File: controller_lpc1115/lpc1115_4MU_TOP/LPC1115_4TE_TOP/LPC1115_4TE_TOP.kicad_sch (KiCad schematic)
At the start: 101 parts, among them P1 ML26, P2 ISP, P3 FE12-1, Q1 BC856, Q2 FZT753, Q3 BC847, U1 LPC1115FBD48, U2 BD9G101, U3 12MHz

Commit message: update all stuff
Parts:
- added D10: 1N4148W, Diode_SMD:D_SOD-123, symbol Diode:1N4148W
- added R3: 390k, Resistor_SMD:R_0805_2012Metric, symbol Device:R
- added R4: 43k, Resistor_SMD:R_0805_2012Metric, symbol Device:R
- C1: value 15nF -> 15n
- C10, C11, C14, C21, C5, C8: value 100nF -> 100n
- C13, C24: value 1uF -> 1u
- C15, C18: value 100pF -> 100p
- C16, C17, C19: value 10nF -> 10n
- C2: value 470n -> 270n; now not fitted
- C22: value 220pF -> 220p
- C3: value VF 100/35 K-D8 -> 100µ/35V
- C4: value 4.7uF 50V -> 4.7µ/35V
- C6: value 47uF 10V -> 47µ/10V
- C7: value 100uF -> 100µ/10V
- D1, D11, D12, D14, D17, D2, D3, D4, D5, D6, D7, D8: value CD4148W -> 1N4148W; footprint Diode_SMD:D_0805_2012Metric -> Diode_SMD:D_SOD-123; symbol Diode:CD4148W -> Diode:1N4148W
- D13: value SMAJ40AC -> SMAJ40CA; now not fitted
- D15, D16: footprint Diode_SMD:D_SOD-123 -> Diode_SMD:D_MiniMELF
- L1: value 4.7uH -> 10u
- P3: now not fitted
- R1: value 24R 2512 1.0W -> 24R 1W
- R17: value 6,2k -> 6k2
- R2: value 1k6 -> 88k7
- R5: value 470R -> 22k1
- U1: value LPC1115FBD48 -> LPC1115FBD48-303
- U2: value BD9G101 -> TPS560430
- renumbered U3 to X1
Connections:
- net +3V3: now also D10.2 (A)
- net EIB_DC: now also R3.2; no longer U2.4 (EN)
- net GND: now also R4.1
- net at C1.2, U2.1 (BOOST): now also D10.1 (K)
- new net: R3.1, R4.2, U2.4 (EN)
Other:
- note added: "für Rohm BD9G101: R22=4k4, R23=680, C16=270n, D7 nicht bestücken für MCP16331: R22=31,25k, R23=10k, C16 nicht bestücken, D7 bestücken für TPS560430: R22=88,7k, R23=22,1k, C16 nicht bestücken, D7 nicht bestücken"
- moved on the sheet: C20, C23, C3, C4, C5, C6, C7, D9, L1, R2, R5

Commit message: fixups for 2MU/4MU controllers - use Seiko oszillator
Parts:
- X1: footprint Oscillator:Oscillator_SMD_EuroQuartz_XO32-4Pin_3.2x2.5mm -> Oscillator:Oscillator_SMD_SeikoEpson_SG210-4Pin_2.5x2.0mm; symbol Oscillator:XO32 -> Oscillator:SG-210STF
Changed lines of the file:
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@@
 		)
 		(instances
-			(project ""
+			(project "LPC1115_4TE_TOP"
 				(path "/4483e78c-ba70-44c8-a665-4aec2a3a71f3"
 					(reference "#FLG02")
@@
 	)
 	(symbol
-		(lib_id "Oscillator:XO32")
+		(lib_id "Oscillator:SG-210STF")
 		(at 170.18 201.93 0)
 		(unit 1)
@@
 		(fields_autoplaced yes)
 		(property "Reference" "X1"
-			(at 172.3741 191.6554 0)
-			(effects
-				(font
-					(size 1.778 1.5113)
-				)
-				(justify left)
+			(at 180.34 193.7065 0)
+			(effects
+				(font
+					(size 1.778 1.5113)
+				)
 			)
 		)
 		(property "Value" "12MHz"
-			(at 172.3741 194.7798 0)
-			(effects
-				(font
-					(size 1.778 1.5113)
-				)
-				(justify left)
-			)
-		)
-		(property "Footprint" "Oscillator:Oscillator_SMD_EuroQuartz_XO32-4Pin_3.2x2.5mm"
-			(at 187.96 210.82 0)
-			(effects
-				(font
-					(size 1.27 1.27)
-				)
-				(hide yes)
-			)
-		)
-		(property "Datasheet" "http://cdn-reichelt.de/documents/datenblatt/B400/XO32.pdf"
+			(at 180.34 197.5165 0)
+			(effects
+				(font
+					(size 1.778 1.5113)
+				)
+			)
+		)
+		(property "Footprint" "Oscillator:Oscillator_SMD_SeikoEpson_SG210-4Pin_2.5x2.0mm"
+			(at 181.61 210.82 0)
+			(effects
+				(font
+					(size 1.27 1.27)
+				)
+				(hide yes)
+			)
+		)
+		(property "Datasheet" "https://support.epson.biz/td/api/doc_check.php?mode=dl&lang=en&Parts=SG-210STF"
 			(at 167.64 201.93 0)
 			(effects
@@
 			)
 		)
-		(property "Description" "HCMOS Clock Oscillator"
+		(property "Description" "CMOS Crystal Oscillator SPXO"
 			(at 170.18 201.93 0)
 			(effects

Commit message: finally standardize selected parts on all boards
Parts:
- C12, C23: value 100nF -> 100n
- C2, D10, D13: now left out of the parts list
- C3: value 100µ/35V -> 100u/35V
- C4: value 4.7µ/35V -> 4.7u/35V
- C6: value 47µ/10V -> 47u/10V
- C7: value 100µ/10V -> 100u/10V
- C9: value 10nF -> 10n
- D9: footprint Diode_SMD:D_SOD-123F -> Diode_SMD:D_SOD-123
- P3: footprint Connector_PinSocket_2.54mm:PinSocket_1x12_P2.54mm_Vertical -> Connector_PinHeader_2.54mm:PinHeader_1x12_P2.54mm_Vertical; now left out of the parts list
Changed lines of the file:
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@@
 			)
 		)
-		(property "Value" "100nF"
+		(property "Value" "100n"
 			(at 191.77 94.8308 90)
 			(effects
@@
 			)
 		)
-		(property "Value" "4.7µ/35V"
+		(property "Value" "4.7u/35V"
 			(at 72.39 52.07 90)
 			(effects
@@
 		(unit 1)
 		(exclude_from_sim no)
-		(in_bom yes)
+		(in_bom no)
 		(on_board yes)
 		(dnp yes)
@@
 		(unit 1)
 		(exclude_from_sim no)
-		(in_bom yes)
+		(in_bom no)
 		(on_board yes)
 		(dnp yes)
@@
 			)
 		)
-		(property "Value" "100µ/35V"
+		(property "Value" "100u/35V"
 			(at 62.23 52.07 90)
 			(effects
@@
 			)
 		)
-		(property "Value" "100nF"
+		(property "Value" "100n"
 			(at 296.799 94.2722 0)
 			(effects
@@
 		(unit 1)
 		(exclude_from_sim no)
-		(in_bom yes)
+		(in_bom no)
 		(on_board yes)
 		(dnp yes)
@@
 			)
 		)
-		(property "Footprint" "Connector_PinSocket_2.54mm:PinSocket_1x12_P2.54mm_Vertical"
+		(property "Footprint" "Connector_PinHeader_2.54mm:PinHeader_1x12_P2.54mm_Vertical"
 			(at 294.64 201.93 0)
 			(effects
@@
 			)
 		)
-		(property "Value" "10nF"
+		(property "Value" "10n"
 			(at 117.856 112.141 0)
 			(effects
@@
 			)
 		)
-		(property "Value" "100µ/10V"
+		(property "Value" "100u/10V"
 			(at 204.851 38.7732 0)
 			(effects
@@
 		(unit 1)
 		(exclude_from_sim no)
-		(in_bom yes)
+		(in_bom no)
 		(on_board yes)
 		(dnp yes)
@@
 			)
 		)
-		(property "Value" "47µ/10V"
+		(property "Value" "47u/10V"
 			(at 163.83 52.07 90)
 			(effects
@@
 			)
 		)
-		(property "Footprint" "Diode_SMD:D_SOD-123F"
+		(property "Footprint" "Diode_SMD:D_SOD-123"
 			(at 130.81 40.64 0)
 			(effects

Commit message: final for manufacturing
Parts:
- R10, R11, R12, R13, R27, R28, R6, R7, R8, R9: value 1k5 -> 1k
- R2: value 88k7 -> 51k
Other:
- note added: "für Rohm BD9G101: R22=4k4, R23=680, C16=270n, D7 nicht bestücken für MCP16331: R22=31,25k, R23=10k, C16 nicht bestücken, D7 bestücken für TPS560430: R22=51k, R23=22,1k, C16 nicht bestücken, D7 nicht bestücken"
- note removed: "für Rohm BD9G101: R22=4k4, R23=680, C16=270n, D7 nicht bestücken für MCP16331: R22=31,25k, R23=10k, C16 nicht bestücken, D7 bestücken für TPS560430: R22=88,7k, R23=22,1k, C16 nicht bestücken, D7 nicht bestücken"
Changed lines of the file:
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@@
 		)
 	)
-	(text "für Rohm BD9G101:\nR22=4k4, R23=680, C16=270n, D7 nicht bestücken\nfür MCP16331:\nR22=31,25k, R23=10k, C16 nicht bestücken, D7 bestücken\nfür TPS560430:\nR22=88,7k, R23=22,1k, C16 nicht bestücken, D7 nicht bestücken"
+	(text "für Rohm BD9G101:\nR22=4k4, R23=680, C16=270n, D7 nicht bestücken\nfür MCP16331:\nR22=31,25k, R23=10k, C16 nicht bestücken, D7 bestücken\nfür TPS560430:\nR22=51k, R23=22,1k, C16 nicht bestücken, D7 nicht bestücken"
 		(exclude_from_sim no)
 		(at 53.34 8.89 0)
@@
 			)
 		)
-		(property "Value" "1k5"
+		(property "Value" "1k"
 			(at 316.738 48.5522 0)
 			(effects
@@
 			)
 		)
-		(property "Value" "1k5"
+		(property "Value" "1k"
 			(at 286.258 48.5522 0)
 			(effects
@@
 			)
 		)
-		(property "Value" "1k5"
+		(property "Value" "1k"
 			(at 225.298 208.5722 0)
 			(effects
@@
 			)
 		)
-		(property "Value" "1k5"
+		(property "Value" "1k"
 			(at 347.218 48.5522 0)
 			(effects
@@
 			)
 		)
-		(property "Value" "1k5"
+		(property "Value" "1k"
 			(at 271.018 48.5522 0)
 			(effects
@@
 			)
 		)
-		(property "Value" "1k5"
+		(property "Value" "1k"
 			(at 255.778 48.5522 0)
 			(effects
@@
 			)
 		)
-		(property "Value" "1k5"
+		(property "Value" "1k"
 			(at 362.458 48.5522 0)
 			(effects
@@
 			)
 		)
-		(property "Value" "1k5"
+		(property "Value" "1k"
 			(at 331.978 48.5522 0)
 			(effects
@@
 			)
 		)
-		(property "Value" "1k5"
+		(property "Value" "1k"
 			(at 243.078 208.5722 0)
 			(effects
@@
 			)
 		)
-		(property "Value" "1k5"
+		(property "Value" "1k"
 			(at 301.498 48.5522 0)
 			(effects
@@
 			)
 		)
-		(property "Value" "88k7"
+		(property "Value" "51k"
 			(at 151.638 33.3122 0)
 			(effects
@@
 		(fields_autoplaced yes)
 		(property "Reference" "X1"
-			(at 180.34 193.7065 0)
+			(at 172.3741 191.6554 0)
 			(effects
 				(font
 					(size 1.778 1.5113)
 				)
+				(justify left)
 			)
 		)
 		(property "Value" "12MHz"
-			(at 180.34 197.5165 0)
+			(at 172.3741 194.7798 0)
 			(effects
 				(font
 					(size 1.778 1.5113)
 				)
+				(justify left)
 			)
 		)

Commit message: update LPC1115_4TE_TOP
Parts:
- C1: value 15n -> 100n
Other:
- note added: "für Rohm BD9G101: R22=4k4, R23=680, C16=270n, D7 nicht bestücken für MCP16331: R22=31,25k, R23=10k, C16 nicht bestücken, D7 bestücken für TPS560430: R22=51k, R23=22,1k, C16 nicht bestücken, D7 nicht bestücken, C1=100n"
- note removed: "für Rohm BD9G101: R22=4k4, R23=680, C16=270n, D7 nicht bestücken für MCP16331: R22=31,25k, R23=10k, C16 nicht bestücken, D7 bestücken für TPS560430: R22=51k, R23=22,1k, C16 nicht bestücken, D7 nicht bestücken"
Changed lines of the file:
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@@
 		)
 	)
-	(text "für Rohm BD9G101:\nR22=4k4, R23=680, C16=270n, D7 nicht bestücken\nfür MCP16331:\nR22=31,25k, R23=10k, C16 nicht bestücken, D7 bestücken\nfür TPS560430:\nR22=51k, R23=22,1k, C16 nicht bestücken, D7 nicht bestücken"
-		(exclude_from_sim no)
-		(at 53.34 8.89 0)
+	(text "für Rohm BD9G101:\nR22=4k4, R23=680, C16=270n, D7 nicht bestücken\nfür MCP16331:\nR22=31,25k, R23=10k, C16 nicht bestücken, D7 bestücken\nfür TPS560430:\nR22=51k, R23=22,1k, C16 nicht bestücken, D7 nicht bestücken, C1=100n"
+		(exclude_from_sim no)
+		(at 46.99 7.62 0)
 		(effects
 			(font
@@
 			)
 		)
-		(property "Value" "15n"
+		(property "Value" "100n"
 			(at 124.46 19.9008 90)
 			(effects

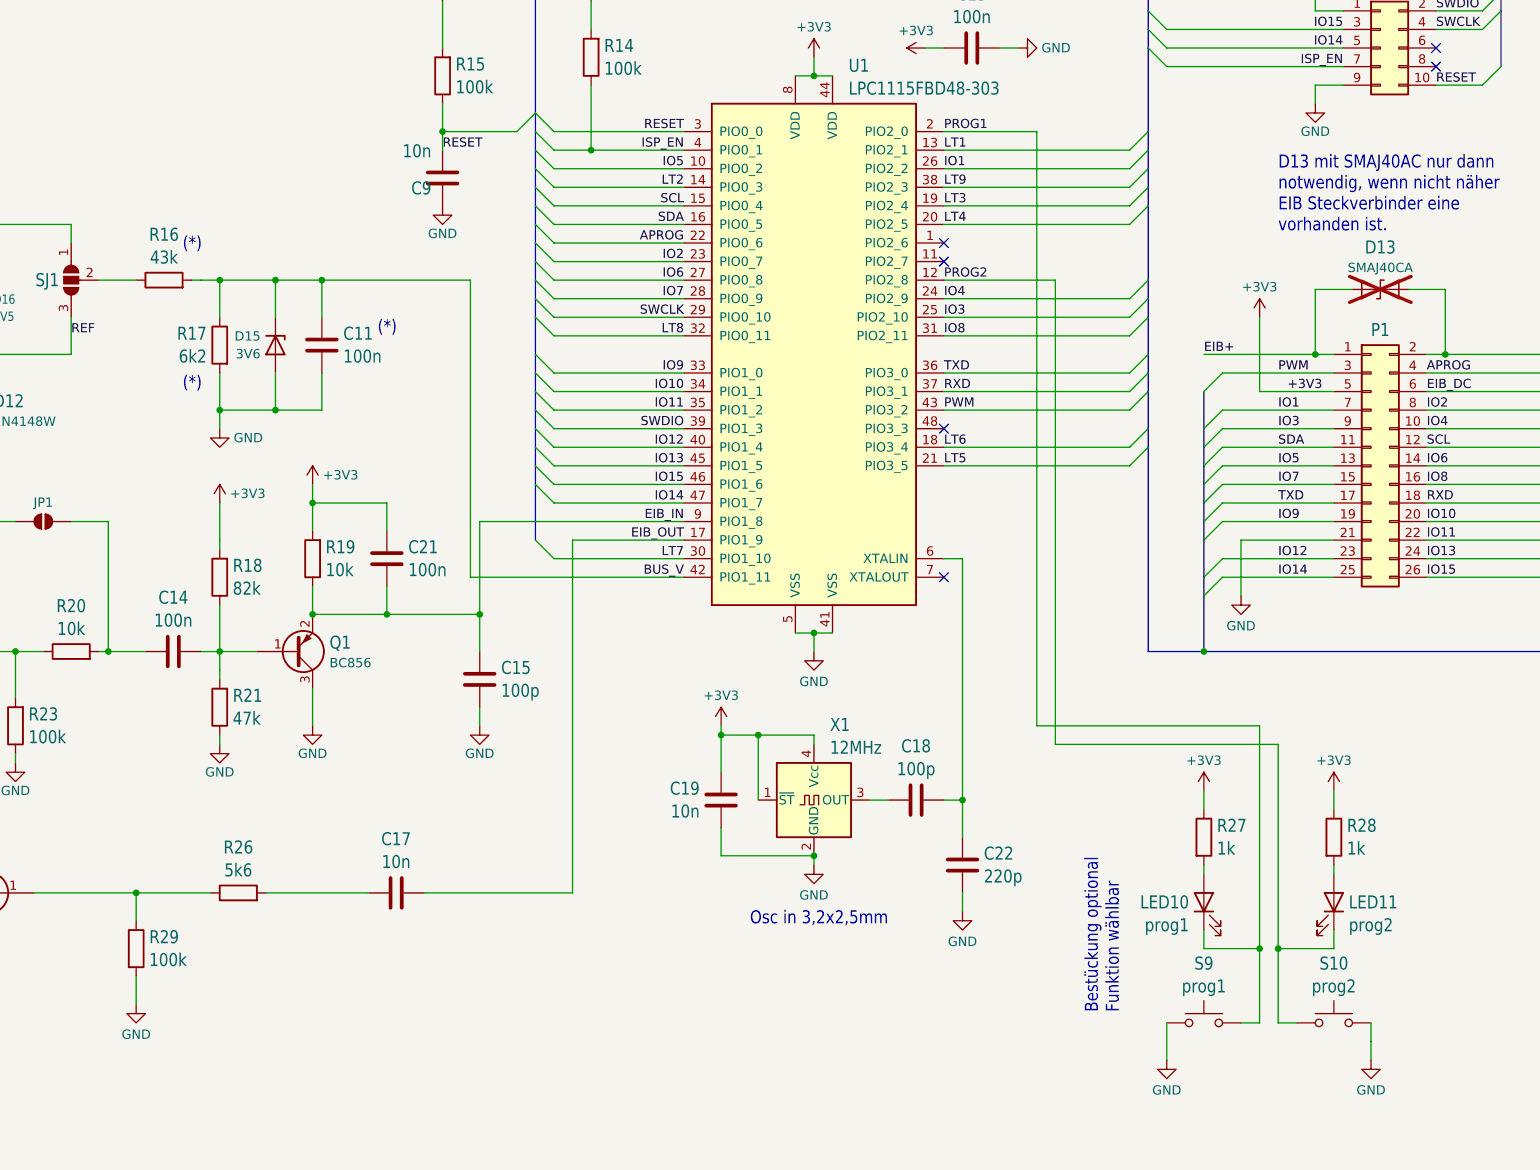
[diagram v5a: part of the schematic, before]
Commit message: update xtal caps, eib_in cap+resistor, bus_v resistors
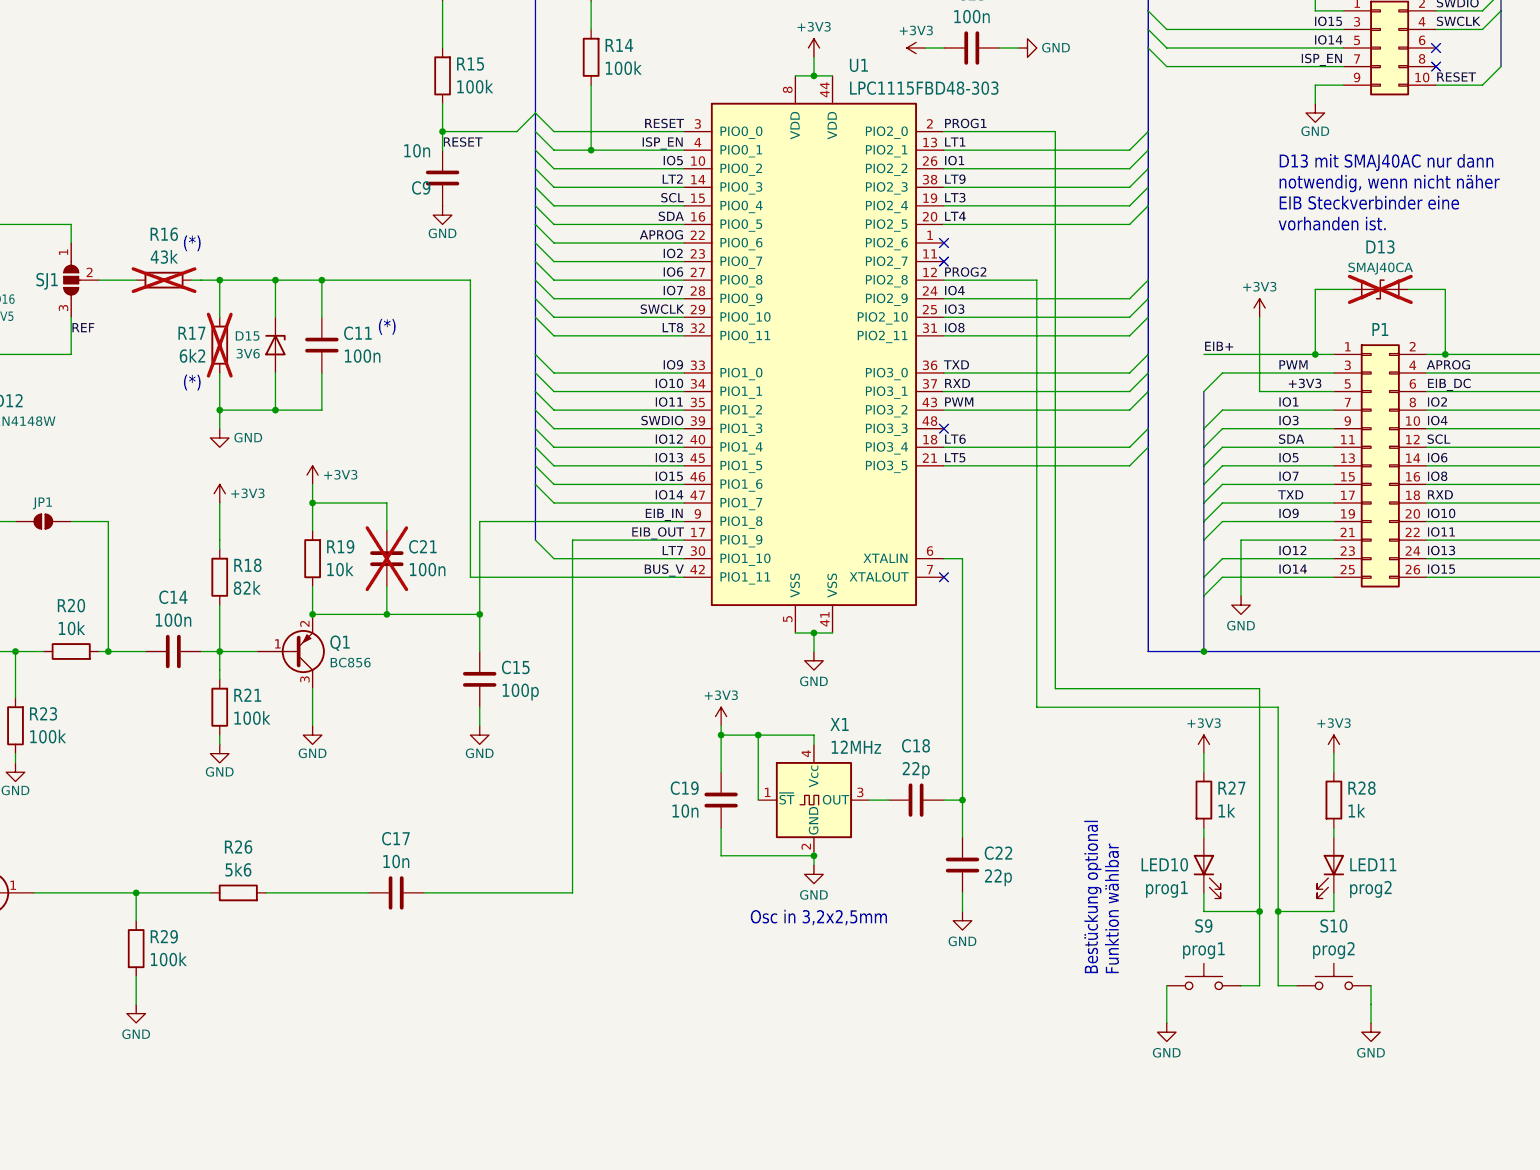
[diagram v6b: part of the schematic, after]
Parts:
- C18: value 100p -> 22p
- C21, R16, R17: now not fitted; now left out of the parts list
- C22: value 220p -> 22p
- R21: value 47k -> 100k
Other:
- moved on the sheet: LED10, LED11, R27, R28, S10, S9

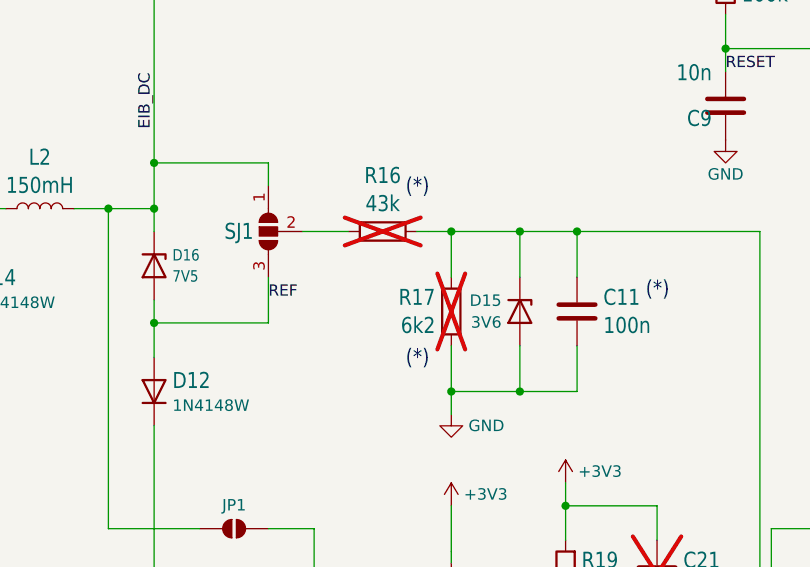
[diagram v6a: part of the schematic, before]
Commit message: controllers: reduce osc load, fix DNP for voltage measurement
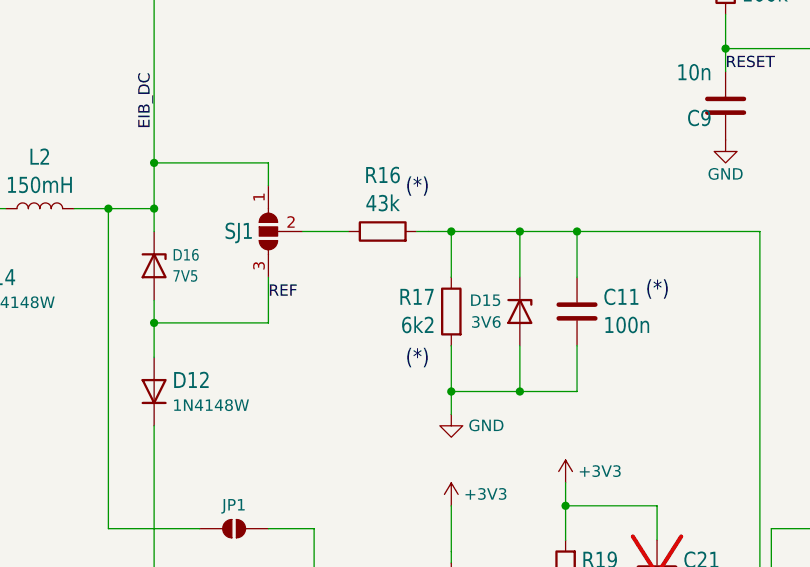
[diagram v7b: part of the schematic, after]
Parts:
- R16, R17: now fitted; now in the parts list
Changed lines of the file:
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@@
 		(unit 1)
 		(exclude_from_sim no)
-		(in_bom no)
-		(on_board yes)
-		(dnp yes)
+		(in_bom yes)
+		(on_board yes)
+		(dnp no)
 		(fields_autoplaced yes)
 		(property "Reference" "R17"
@@
 		(unit 1)
 		(exclude_from_sim no)
-		(in_bom no)
-		(on_board yes)
-		(dnp yes)
+		(in_bom yes)
+		(on_board yes)
+		(dnp no)
 		(fields_autoplaced yes)
 		(property "Reference" "R16"
